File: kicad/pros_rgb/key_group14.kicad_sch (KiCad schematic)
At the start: 13 parts

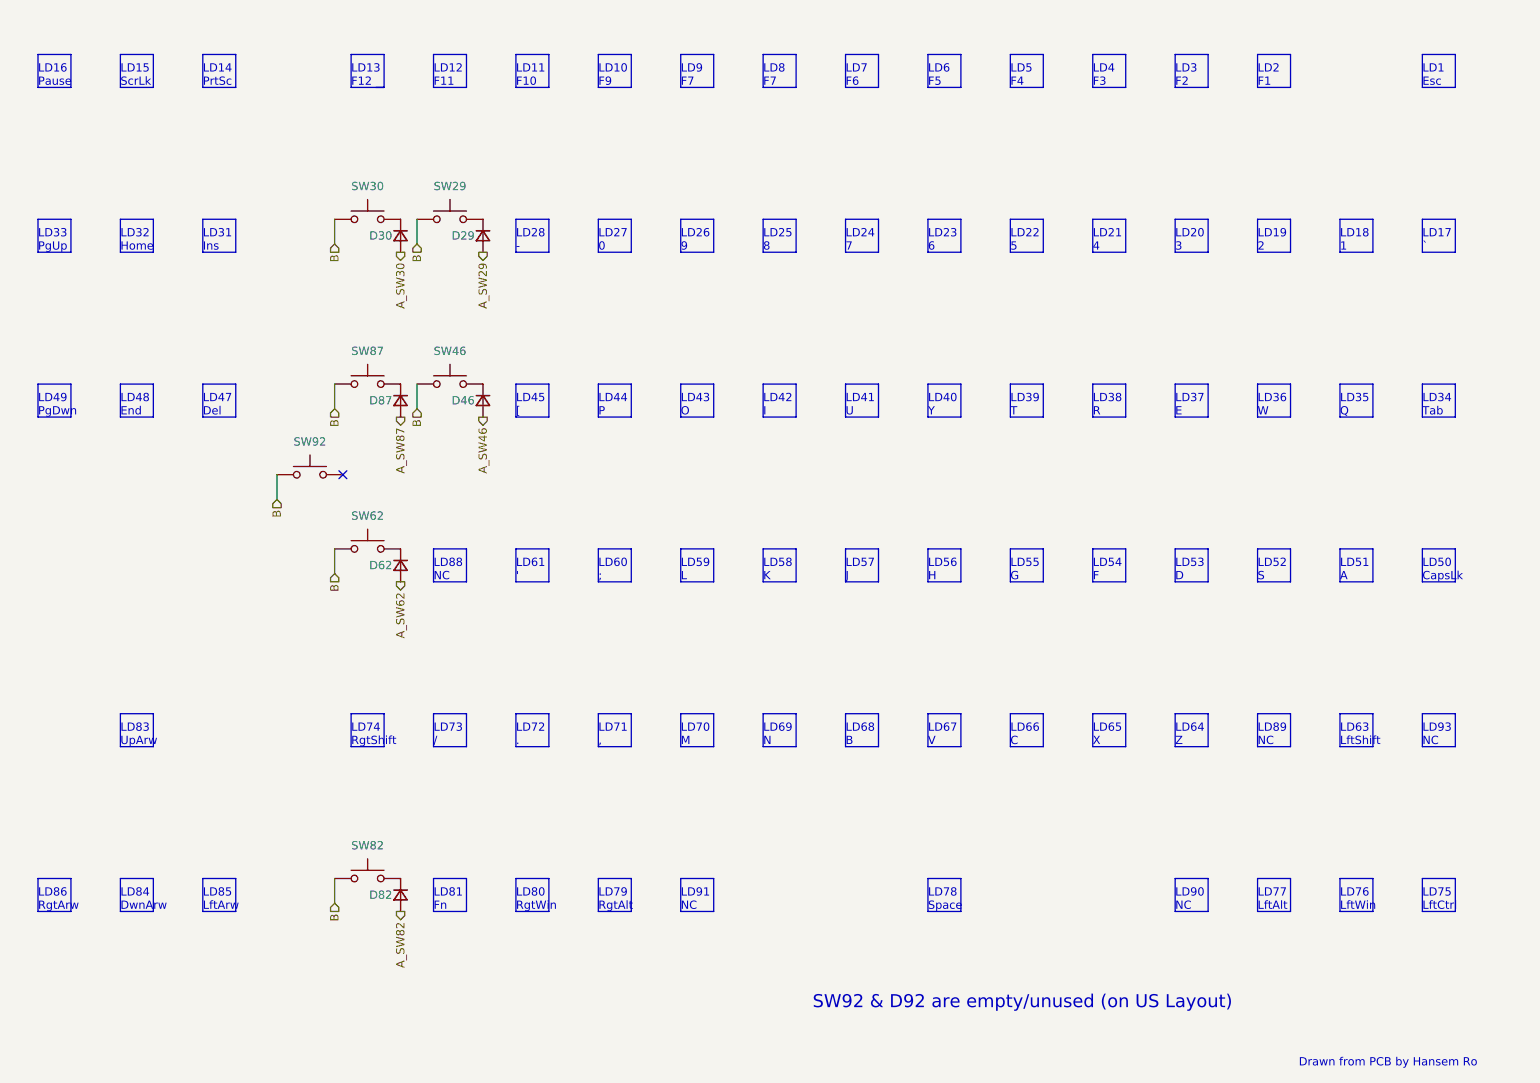
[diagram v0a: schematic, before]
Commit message: kicad/pros_rgb: update key groupings
These new groupings are based off ordering in firmware:
https://github.com/hansemro/pok3r_re_firmware/blob/4b68aa4baf7d28dc8dbf8eebcb1fdb59e7bcd629/disassemble/cmprosrgb/v122/cmprosrgb_v122.txt#L14599-L14629
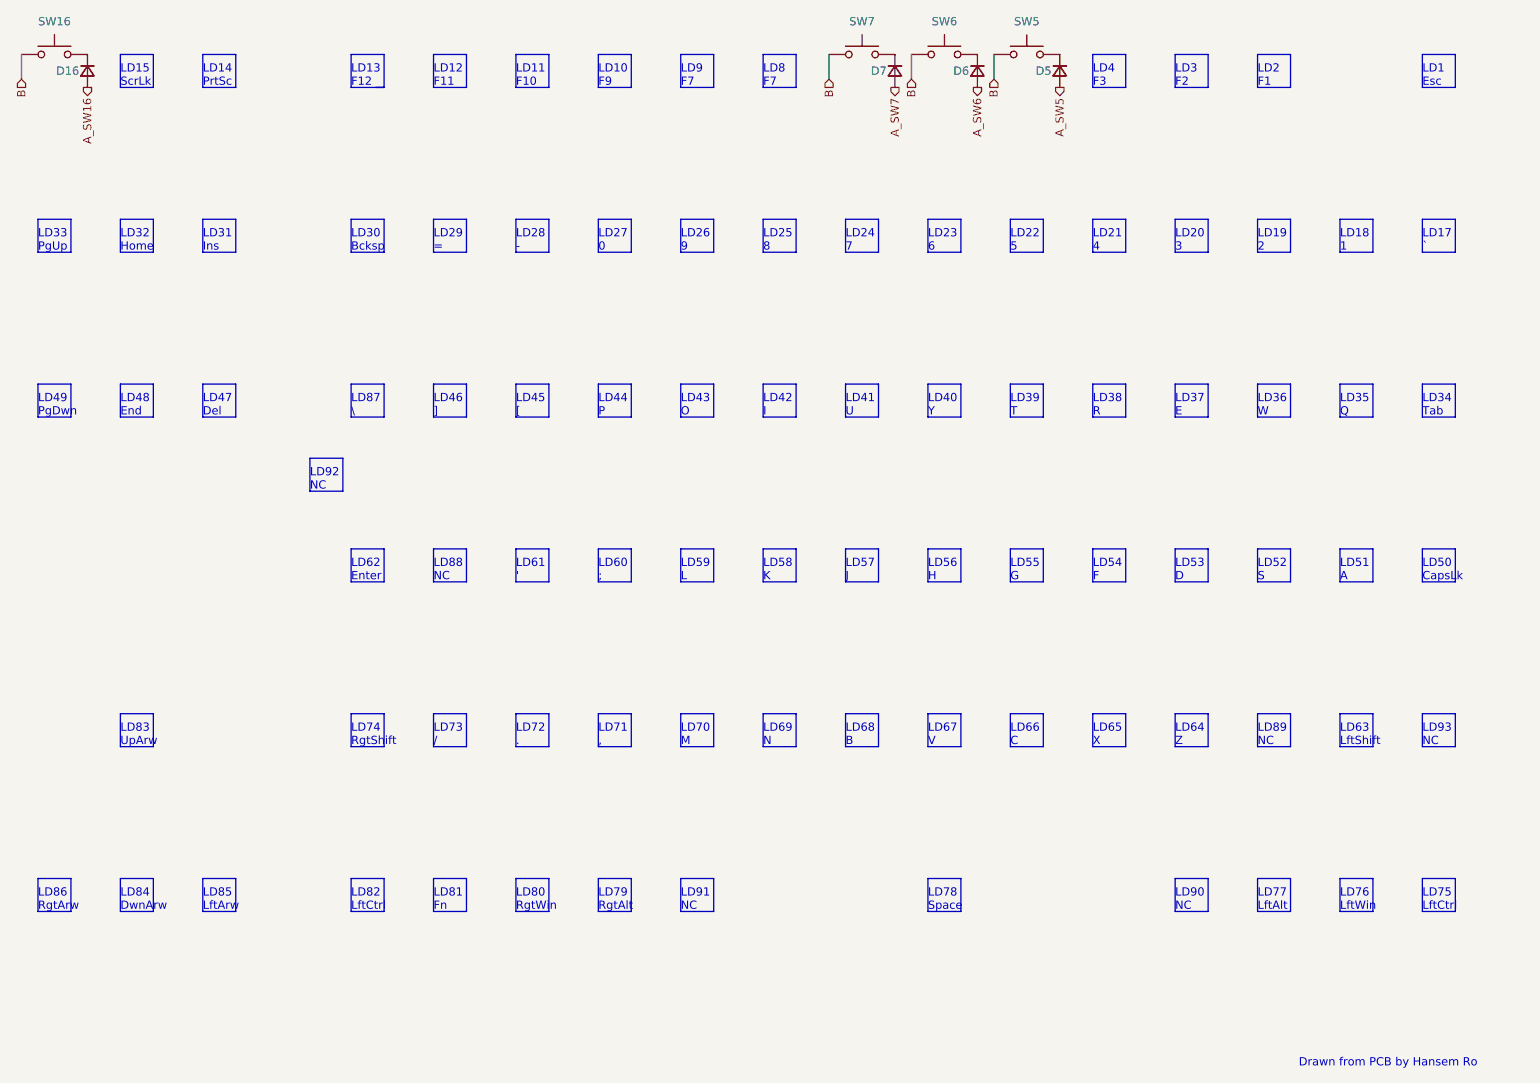
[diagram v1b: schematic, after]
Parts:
- removed D29, D30, D46, D62, D82, D87: ~, symbol Device:D_Small
- removed SW29, SW30, SW46, SW62, SW82, SW87, SW92: ~, symbol Switch:SW_Push
- added D16, D5, D6, D7: (no value), symbol Device:D_Small
- added SW16, SW5, SW6, SW7: (no value), symbol Switch:SW_Push
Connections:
- net B: now also SW16.1, SW5.1, SW6.1, SW7.1
- new net: D6.1 (K), SW6.2
- new net: D7.1 (K), SW7.2
- new net: D5.1 (K), SW5.2
- new net: D16.1 (K), SW16.2
- new net A_SW16: D16.2 (A)
- new net A_SW5: D5.2 (A)
- new net A_SW6: D6.2 (A)
- new net A_SW7: D7.2 (A)
- no-connect marks 1 -> 0
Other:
- note added: "LD29 ="
- note added: "LD30 Bcksp"
- note added: "LD46 ]"
- note added: "LD62 Enter"
- note added: "LD82 LftCtrl"
- note added: "LD87 \"
- note added: "LD92 NC"
- note removed: "LD16 Pause"
- note removed: "LD5 F4"
- note removed: "LD6 F5"
- note removed: "LD7 F6"
- note removed: "SW92 & D92 are empty/unused (on US Layout)"

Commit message: kicad/pros_rgb: mark as Rev. B
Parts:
- D16, D5, D6, D7, SW16, SW5, SW6, SW7: value (none) -> ~
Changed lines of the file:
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@@
       (effects (font (size 1.27 1.27)) (justify right))
     )
-    (property "Value" "" (id 1) (at 205.74 27.9399 90)
+    (property "Value" "~" (id 1) (at 205.74 27.9399 90)
       (effects (font (size 1.27 1.27)) (justify left))
     )
@@
     (in_bom yes) (on_board yes)
     (property "Reference" "SW7" (id 0) (at 185.42 19.05 0))
-    (property "Value" "" (id 1) (at 185.42 19.05 0))
+    (property "Value" "~" (id 1) (at 185.42 19.05 0))
     (property "Footprint" "" (id 2) (at 185.42 19.05 0)
       (effects (font (size 1.27 1.27)) hide)
@@
       (effects (font (size 1.27 1.27)) (justify right))
     )
-    (property "Value" "" (id 1) (at 193.04 27.9399 90)
+    (property "Value" "~" (id 1) (at 193.04 27.9399 90)
       (effects (font (size 1.27 1.27)) (justify left))
     )
@@
       (effects (font (size 1.27 1.27)) (justify right))
     )
-    (property "Value" "" (id 1) (at 218.44 27.9399 90)
+    (property "Value" "~" (id 1) (at 218.44 27.9399 90)
       (effects (font (size 1.27 1.27)) (justify left))
     )
@@
     (in_bom yes) (on_board yes)
     (property "Reference" "SW16" (id 0) (at 60.96 19.05 0))
-    (property "Value" "" (id 1) (at 60.96 19.05 0))
+    (property "Value" "~" (id 1) (at 60.96 19.05 0))
     (property "Footprint" "" (id 2) (at 60.96 19.05 0)
       (effects (font (size 1.27 1.27)) hide)
@@
     (in_bom yes) (on_board yes)
     (property "Reference" "SW6" (id 0) (at 198.12 19.05 0))
-    (property "Value" "" (id 1) (at 198.12 19.05 0))
+    (property "Value" "~" (id 1) (at 198.12 19.05 0))
     (property "Footprint" "" (id 2) (at 198.12 19.05 0)
       (effects (font (size 1.27 1.27)) hide)
@@
     (in_bom yes) (on_board yes)
     (property "Reference" "SW5" (id 0) (at 210.82 19.05 0))
-    (property "Value" "" (id 1) (at 210.82 19.05 0))
+    (property "Value" "~" (id 1) (at 210.82 19.05 0))
     (property "Footprint" "" (id 2) (at 210.82 19.05 0)
       (effects (font (size 1.27 1.27)) hide)
@@
       (effects (font (size 1.27 1.27)) (justify right))
     )
-    (property "Value" "" (id 1) (at 68.58 27.9399 90)
+    (property "Value" "~" (id 1) (at 68.58 27.9399 90)
       (effects (font (size 1.27 1.27)) (justify left))
     )

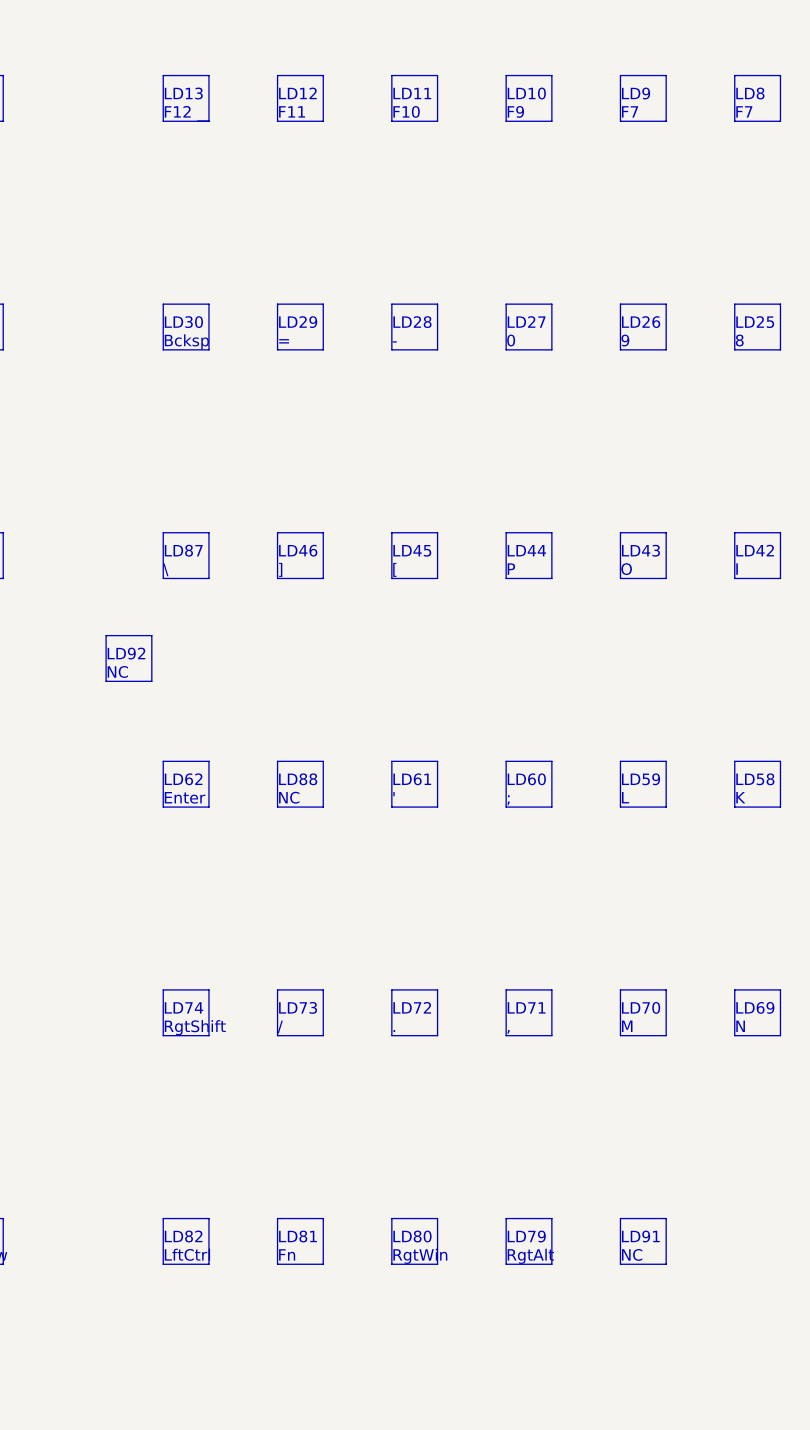
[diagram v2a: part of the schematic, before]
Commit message: kicad/pros_rgb: fix typos
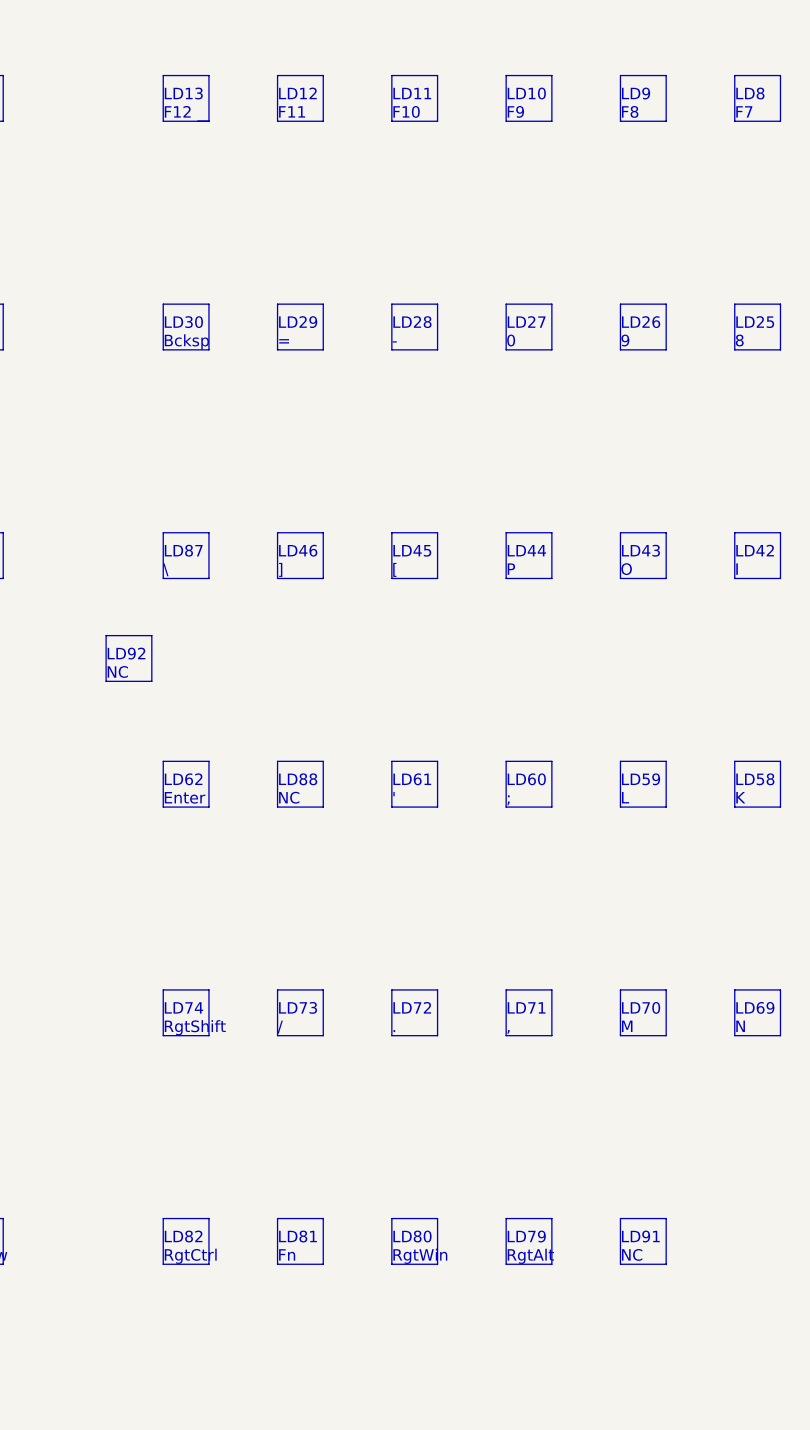
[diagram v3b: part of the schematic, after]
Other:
- note added: "LD82 RgtCtrl"
- note added: "LD9 F8"
- note removed: "LD82 LftCtrl"
- note removed: "LD9 F7"
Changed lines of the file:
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@@
     (effects (font (size 1.27 1.27)) (justify left bottom))
   )
-  (text "LD9\nF7" (at 157.48 29.21 0)
+  (text "LD9\nF8" (at 157.48 29.21 0)
     (effects (font (size 1.27 1.27)) (justify left bottom))
   )
@@
     (effects (font (size 1.27 1.27)) (justify left bottom))
   )
-  (text "LD82\nLftCtrl" (at 106.68 156.21 0)
+  (text "LD82\nRgtCtrl" (at 106.68 156.21 0)
     (effects (font (size 1.27 1.27)) (justify left bottom))
   )
